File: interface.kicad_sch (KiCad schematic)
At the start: 168 parts, among them IC107 RC4558, IC3 M51131L, IC501 D91317GD, IC502 MSM5205, IC503 RC4558, IC504 4053, IC521 RC4558, Q102 26, Q606 15, Q608 AAR 29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

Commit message: Add more capacitor values, rearrange some schematics.
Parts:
- C105: value ? -> ? 1uF
- C105: value ? -> ? 1nF
- RA501, RA502, RA503, RA504: value R_Pack04 -> 4x4.7K
- RA511, RA512, RA513: value R_Pack04 -> 4x47K
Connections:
- net BAL_L: no longer names the net of C105.2, IC3.3 (OUT1)
- net BAL_R: no longer names the net of C105.2, IC3.13 (OUT2)
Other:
- moved on the sheet: C105, D601, D602, IC107A, IC107B, IC3, IC503A, IC503B, IC504, IC521A, IC521B, JK602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

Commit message: Add markings for SMD Ds and Qs.
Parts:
- D601: value P -> P 30
- Q1: value ~ -> BR 29
- Q1: value ~ -> AAR 29
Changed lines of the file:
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@@
       (effects (font (size 1.27 1.27)) (justify left))
     )
-    (property "Value" "~" (at 72.39 359.41 0)
+    (property "Value" "BR 29" (at 72.39 359.41 0)
       (effects (font (size 1.27 1.27)) (justify left))
     )
@@
       (effects (font (size 1.27 1.27)) (justify left))
     )
-    (property "Value" "P" (at 493.395 80.645 90)
+    (property "Value" "P 30" (at 493.395 80.645 90)
       (effects (font (size 1.27 1.27)) (justify left))
     )
@@
       (effects (font (size 1.27 1.27)) (justify left))
     )
-    (property "Value" "~" (at 542.925 94.615 0)
+    (property "Value" "AAR 29" (at 542.925 94.615 0)
       (effects (font (size 1.27 1.27)) (justify left))
     )
@@
       (effects (font (size 1.27 1.27)) (justify left))
     )
-    (property "Value" "~" (at 543.56 63.5 0)
-      (effects (font (size 1.27 1.27)) (justify left))
-    )
+    (property "Value" "AAR 29" (at 543.56 63.5 0)
+      (effects (font (size 1.27 1.27)) (justify left))
+    )

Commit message: More schematic clean-up/annotation.
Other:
- note added: "ADPCM"
- note added: "Audio MUX/DEMUX"
- note added: "Main ASIC responsible for communication between PC Engine and CD-ROM."
- note added: "Volume Balance"
- company: (none) -> By Cosam
- title: (none) -> PC Engine Duo Integrated IFU equivalent
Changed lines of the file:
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@@
   (paper "A2")
   (title_block
-    (date "2023-11-01")
-    (rev "1.0")
-    (comment 1 "Reverse engineered from original PWA-3285-A board by Cosam")
-    (comment 3 "WORK IN PROGRESS")
+    (title "PC Engine Duo Integrated IFU equivalent")
+    (date "2023-11-03")
+    (rev "1.1")
+    (company "By Cosam")
+    (comment 1 "https://github.com/Board-Folk/PC-Engine-Duo")
+    (comment 2 "For contributions or corrections please visit:")
+    (comment 3 "Additional parts reverse engineered from original PWA-3285-A board.")
+    (comment 4 "Parts common to PC Engine adapted from TurboGrafx-16 schematics.")
   )
   (junction (at 548.64 234.315) (diameter 0) (color 0 0 0 0)
@@
   (junction (at 447.04 41.275) (diameter 0) (color 0 0 0 0)
   )
-  (junction (at 43.815 187.325) (diameter 0) (color 0 0 0 0)
-  )
   (junction (at 367.03 373.38) (diameter 0) (color 0 0 0 0)
   )
@@
     (stroke (width 0) (type default))
   )
-  (wire (pts (xy 342.265 81.28) (xy 342.265 82.55))
+  (wire (pts (xy 342.265 78.105) (xy 342.265 82.55))
     (stroke (width 0) (type default))
   )
@@
     (stroke (width 0) (type default))
   )
-  (wire (pts (xy 44.45 187.325) (xy 43.815 187.325))
-    (stroke (width 0) (type default))
-  )
   (wire (pts (xy 168.275 139.065) (xy 186.055 139.065))
     (stroke (width 0) (type default))
@@
     (stroke (width 0) (type default))
   )
+  (text "Main ASIC responsible for\ncommunication between\nPC Engine and CD-ROM."
+    (at 104.14 126.365 0)
+    (effects (font (size 1.27 1.27)) (justify left bottom))
+  )
+  (text "Audio MUX/DEMUX" (at 286.385 206.375 0)
+    (effects (font (size 1.27 1.27)) (justify left bottom))
+  )
+  (text "ADPCM" (at 117.475 248.285 0)
+    (effects (font (size 2.54 2.54)) (justify left bottom))
+  )
+  (text "Volume\nBalance" (at 352.425 95.25 0)
+    (effects (font (size 1.27 1.27)) (justify left bottom))
+  )
   (label "XA3" (at 62.865 93.345 0) (fields_autoplaced)
     (effects (font (size 1.27 1.27)) (justify left bottom))
@@
     )
   )
-  (symbol (lib_id "power:+5VP") (at 342.265 81.28 0) (unit 1)
+  (symbol (lib_id "power:+5VP") (at 342.265 78.105 0) (unit 1)
     (in_bom yes) (on_board yes) (dnp no) (fields_autoplaced)
-    (property "Reference" "#PWR0112" (at 342.265 85.09 0)
+    (property "Reference" "#PWR0112" (at 342.265 81.915 0)
       (effects (font (size 1.27 1.27)) hide)
     )
-    (property "Value" "+5VP" (at 342.265 76.835 0)
+    (property "Value" "+5VP" (at 342.265 73.66 0)
       (effects (font (size 1.27 1.27)))
     )
-    (property "Footprint" "" (at 342.265 81.28 0)
+    (property "Footprint" "" (at 342.265 78.105 0)
       (effects (font (size 1.27 1.27)) hide)
     )
-    (property "Datasheet" "" (at 342.265 81.28 0)
+    (property "Datasheet" "" (at 342.265 78.105 0)
       (effects (font (size 1.27 1.27)) hide)
     )
@@
   )
   (symbol (lib_id "PC-Engine:D91317GD_Labeled") (at 118.745 142.875 0) (unit 1)
-    (in_bom yes) (on_board yes) (dnp no) (fields_autoplaced)
-    (property "Reference" "IC501" (at 148.9711 207.645 0)
+    (in_bom yes) (on_board yes) (dnp no)
+    (property "Reference" "IC501" (at 154.305 210.185 0)
       (effects (font (size 1.27 1.27)) (justify left))
     )
-    (property "Value" "D91317GD" (at 148.9711 210.185 0)
+    (property "Value" "D91317GD" (at 154.305 212.725 0)
       (effects (font (size 1.27 1.27)) (justify left))
     )
@@
       (effects (font (size 1.27 1.27)) (justify left))
     )
-    (property "Value" "BR 29" (at 72.39 359.41 0)
+    (property "Value" "BR 29" (at 60.325 365.76 0)
       (effects (font (size 1.27 1.27)) (justify left))
     )
@@
   (symbol (lib_id "PC-Engine:M51131L") (at 342.265 110.49 0) (unit 1)
     (in_bom yes) (on_board yes) (dnp no)
-    (property "Reference" "IC3" (at 347.98 79.375 0)
+    (property "Reference" "IC3" (at 346.075 81.915 0)
       (effects (font (size 1.27 1.27)) (justify left))
     )
-    (property "Value" "M51131L" (at 351.155 81.915 0)
+    (property "Value" "M51131L" (at 349.25 84.455 0)
       (effects (font (size 1.27 1.27)))
     )
@@
   )
   (symbol (lib_id "Device:Q_PNP_CBE") (at 67.31 318.77 0) (mirror x) (unit 1)
-    (in_bom yes) (on_board yes) (dnp no) (fields_autoplaced)
-    (property "Reference" "Q606" (at 73.025 320.04 0)
+    (in_bom yes) (on_board yes) (dnp no)
+    (property "Reference" "Q606" (at 73.66 316.23 0)
       (effects (font (size 1.27 1.27)) (justify left))
     )
-    (property "Value" "15" (at 73.025 317.5 0)
+    (property "Value" "15" (at 73.66 318.77 0)
       (effects (font (size 1.27 1.27)) (justify left))
     )
@@
   )
   (symbol (lib_id "Device:Q_NPN_CBE") (at 537.845 93.345 0) (unit 1)
-    (in_bom yes) (on_board yes) (dnp no) (fields_autoplaced)
-    (property "Reference" "Q1" (at 542.925 93.345 0)
+    (in_bom yes) (on_board yes) (dnp no)
+    (property "Reference" "Q1" (at 542.925 92.075 0)
       (effects (font (size 1.27 1.27)) (justify left))
     )
@@
   )
   (symbol (lib_id "Device:Q_NPN_CBE") (at 538.48 62.23 0) (unit 1)
-    (in_bom yes) (on_board yes) (dnp no) (fields_autoplaced)
-    (property "Reference" "Q1" (at 543.56 62.23 0)
+    (in_bom yes) (on_board yes) (dnp no)
+    (property "Reference" "Q1" (at 543.56 60.96 0)
       (effects (font (size 1.27 1.27)) (justify left))
     )

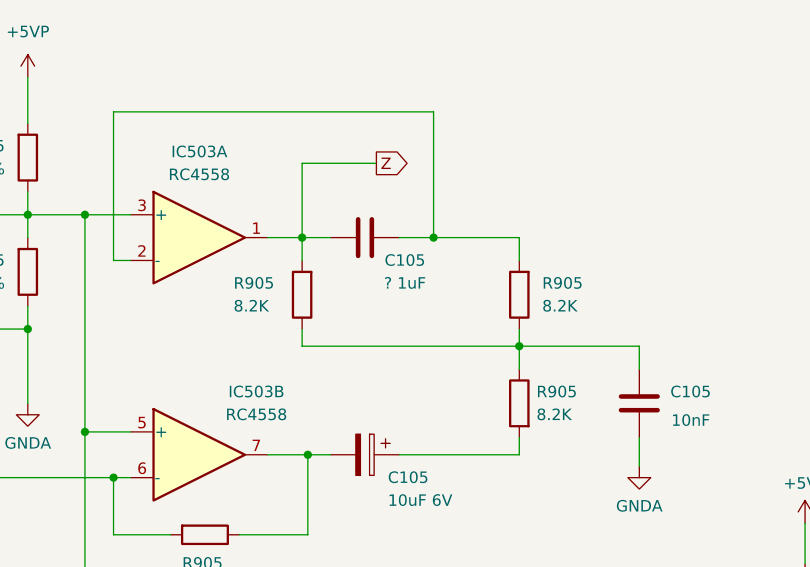
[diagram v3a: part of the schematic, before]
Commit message: Correct some values/references.
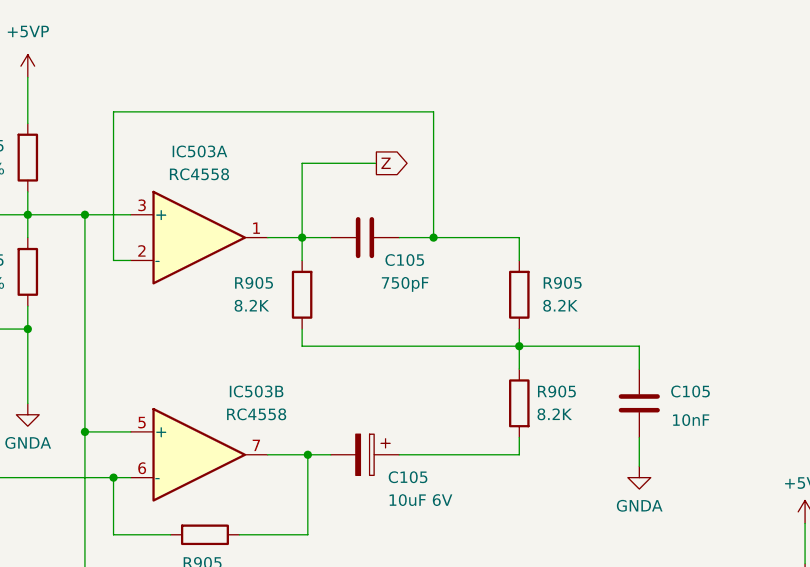
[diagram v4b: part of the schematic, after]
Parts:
- C105: value ? 1uF -> 750pF
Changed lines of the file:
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@@
       (effects (font (size 1.27 1.27)))
     )
-    (property "Value" "? 1uF" (at 297.815 51.435 90)
+    (property "Value" "750pF" (at 297.815 51.435 90)
       (effects (font (size 1.27 1.27)))
     )

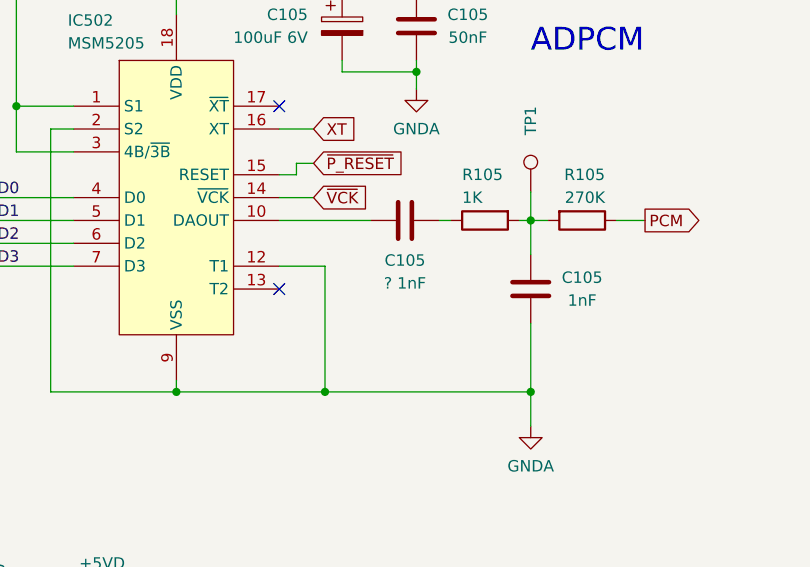
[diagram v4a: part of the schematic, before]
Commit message: Minor footprint and silkscreen changes/corrections.
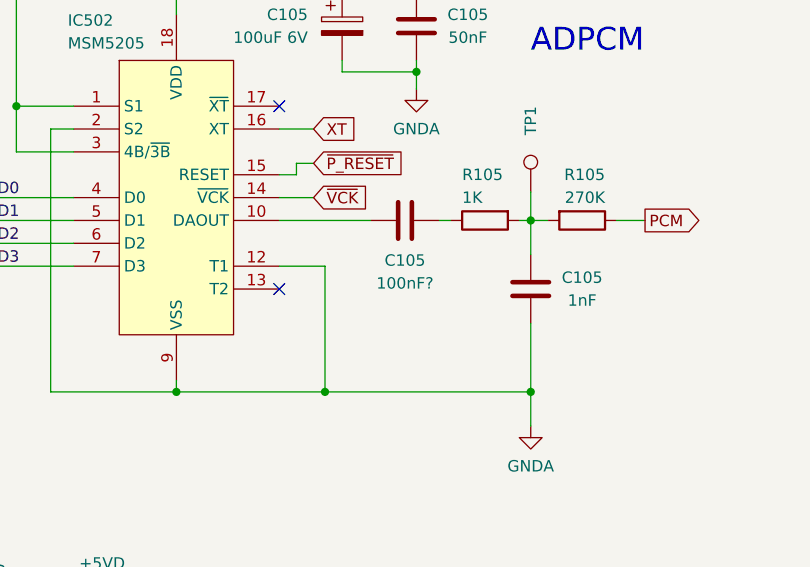
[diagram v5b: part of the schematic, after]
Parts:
- C105: value ? 1nF -> 100nF?
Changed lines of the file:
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@@
     (title "PC Engine Duo Integrated IFU equivalent")
     (date "2023-11-03")
-    (rev "1.1")
+    (rev "1.2")
     (company "By Cosam")
     (comment 1 "https://github.com/Board-Folk/PC-Engine-Duo")
     (comment 2 "For contributions or corrections please visit:")
-    (comment 3 "Additional parts reverse engineered from original PWA-3285-A board.")
+    (comment 3 "Additional parts reverse engineered from original PWA-3285-A 72932851 board.")
     (comment 4 "Parts common to PC Engine adapted from TurboGrafx-16 schematics.")
   )
@@
       (effects (font (size 1.27 1.27)))
     )
-    (property "Value" "? 1nF" (at 103.505 273.685 90)
+    (property "Value" "100nF?" (at 103.505 273.685 90)
       (effects (font (size 1.27 1.27)))
     )

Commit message: Minor schematic/silkscreen changes.
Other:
- note added: "Headphones"
- moved on the sheet: C105, D602, IC107A, IC107B, IC502, IC504, JK602, L106, Q1, Q606, Q608, Q609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

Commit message: Refresh Gerbers and iBOM.
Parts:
- R905: value 47K? -> 47K
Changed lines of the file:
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@@
   (symbol (lib_id "Device:R") (at 311.15 127 0) (unit 1)
     (in_bom yes) (on_board yes) (dnp no)
-    (property "Reference" "R905" (at 308.61 128.27 0)
-      (effects (font (size 1.27 1.27)) (justify right))
-    )
-    (property "Value" "47K?" (at 308.61 125.73 0)
+    (property "Reference" "R905" (at 308.61 125.73 0)
+      (effects (font (size 1.27 1.27)) (justify right))
+    )
+    (property "Value" "47K" (at 308.61 128.27 0)
       (effects (font (size 1.27 1.27)) (justify right))
     )
@@
   (symbol (lib_id "Device:R") (at 311.15 137.16 0) (unit 1)
     (in_bom yes) (on_board yes) (dnp no)
-    (property "Reference" "R905" (at 308.61 138.43 0)
-      (effects (font (size 1.27 1.27)) (justify right))
-    )
-    (property "Value" "47K?" (at 308.61 135.89 0)
-      (effects (font (size 1.27 1.27)) (justify right))
-    )
+    (property "Reference" "R905" (at 308.61 135.89 0)
+      (effects (font (size 1.27 1.27)) (justify right))
+    )
+    (property "Value" "47K" (at 308.61 138.43 0)
+      (effects (font (size 1.27 1.27)) (justify right))
+    )
